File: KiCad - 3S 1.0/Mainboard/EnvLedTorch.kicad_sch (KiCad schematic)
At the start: 135 parts, among them IC1 BQ25792RQMR, IC2 TPS25750DRJKR, J1 HRO_TYPE-C-31-M-12, J10 3S/1.5MHz/1A ICGH, J11 4S/1.5MHz/1A ICGH, J2 Conn_01x02, J3 Aardvark, J4 SYS/GND, J5 BAT/GND, J6 Aardvark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

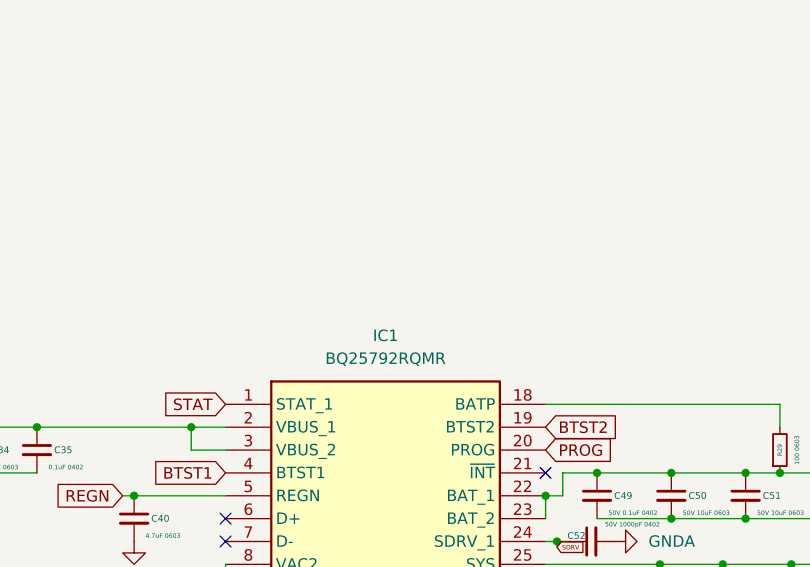
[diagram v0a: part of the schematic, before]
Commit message: Added a note in schematic, Current version is capable of 45W and isnt advised for 65W or more, I should change the IC out.
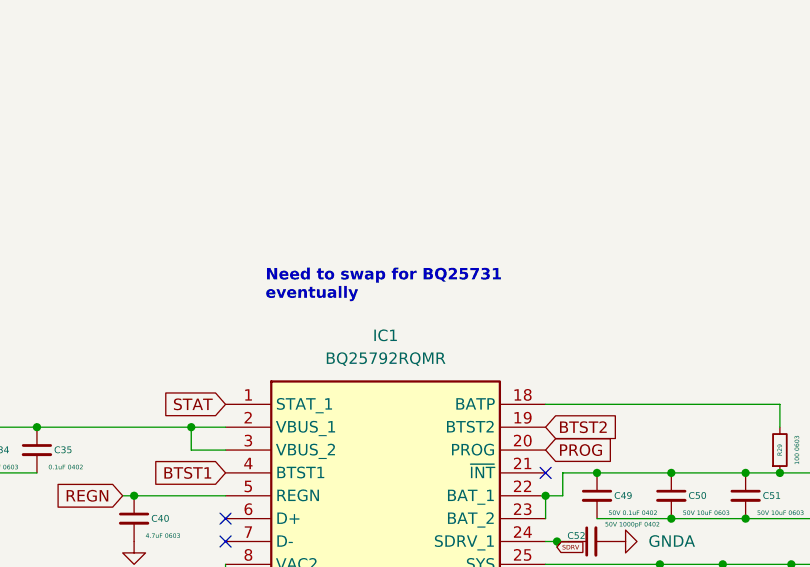
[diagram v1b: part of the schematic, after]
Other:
- note added: "Need to swap for BQ25731 eventually"
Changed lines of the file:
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@@
     (effects (font (size 1.27 1.27)) (justify left bottom))
+  )
+  (text "Need to swap for BQ25731\neventually" (at 287.02 92.71 0)
+    (effects (font (size 1.27 1.27) (thickness 0.254) bold) (justify left bottom))
   )
   (text "RVSS" (at 194.31 273.685 0)
